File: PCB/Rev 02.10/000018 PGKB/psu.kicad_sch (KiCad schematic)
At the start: 11 parts, among them U6 MCP1825T-3302E/DC, U7 CAT811TTBI-GT3

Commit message: Maybe new psu needed
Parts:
- added U8: DC_DC_3V3_OKI-78SR-3.3/1.5-W36H-C, KD_Power_Supply:Converter_DCDC_Murata_OKI-78SR_Horizontal, symbol KD_Power_Supply:DC_DC_3V3_OKI-78SR-3.3/1.5-W36H-C
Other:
- note added: "Bigger PSU needed?"

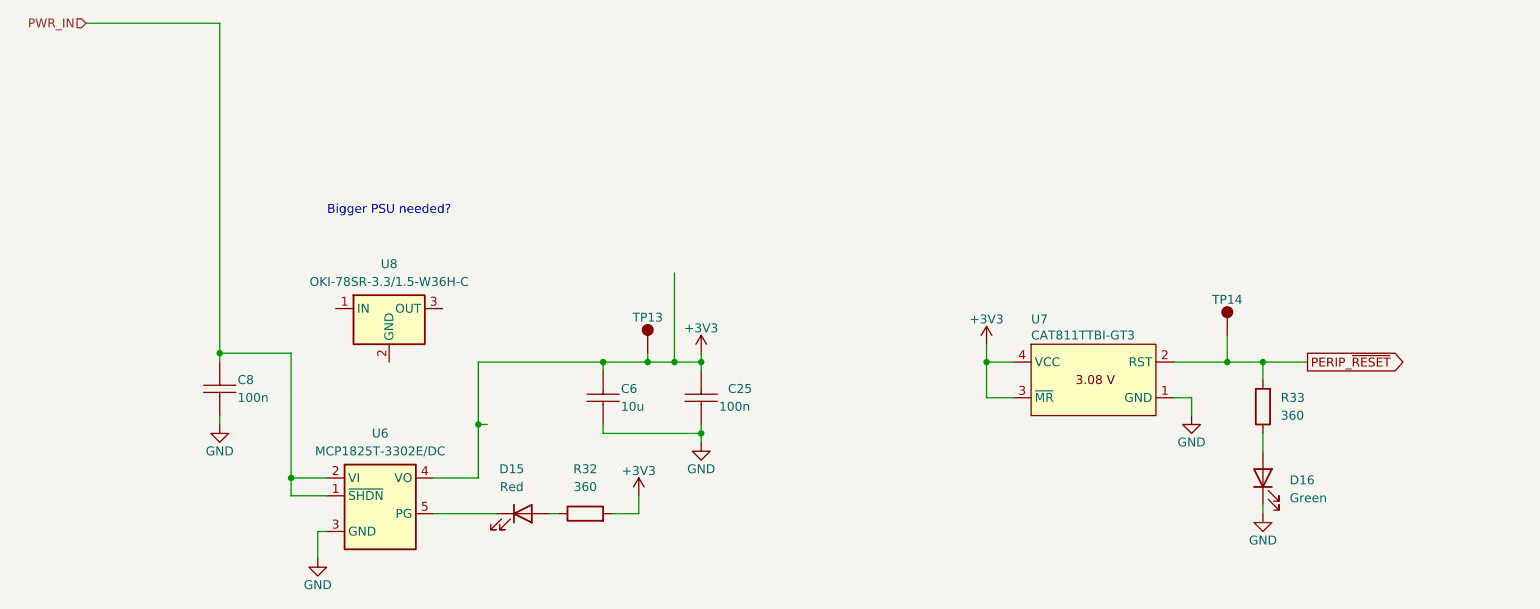
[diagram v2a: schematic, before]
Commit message: Bugfixes for Rev 2
Oscillator, USB reversed, USB series resistors values
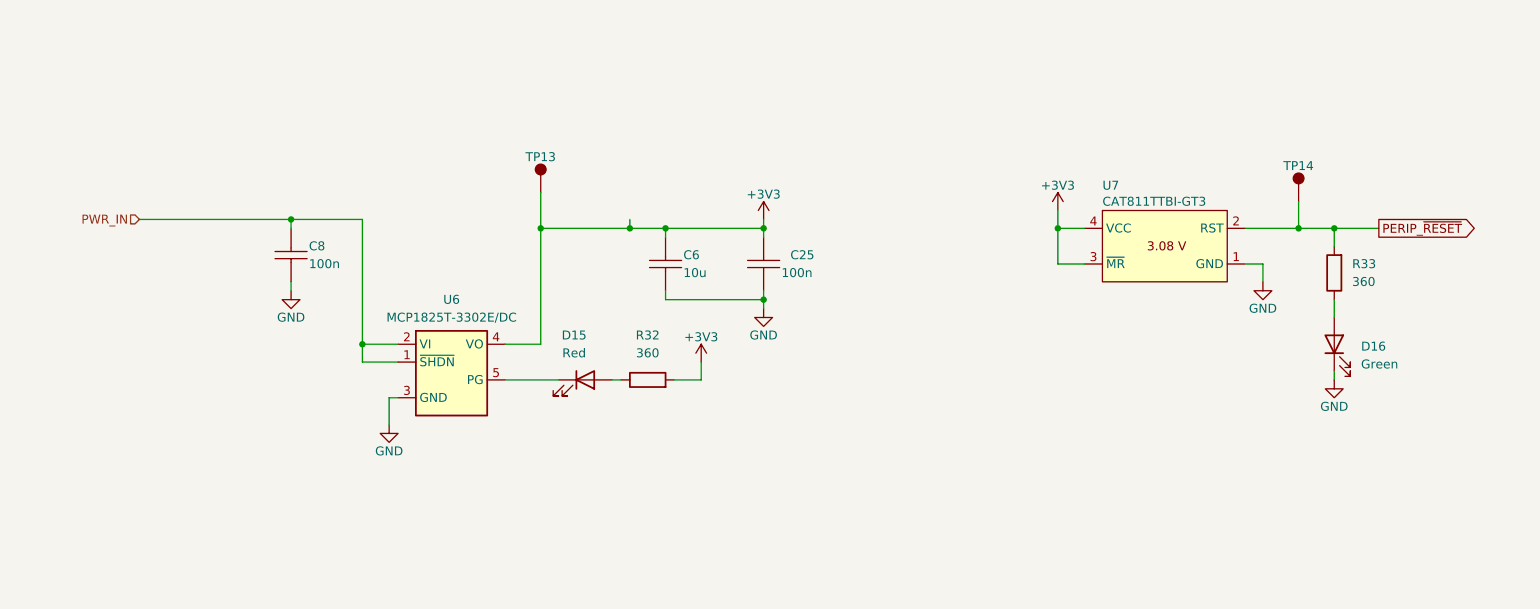
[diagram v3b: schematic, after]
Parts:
- removed U8: DC_DC_3V3_OKI-78SR-3.3/1.5-W36H-C, KD_Power_Supply:Converter_DCDC_Murata_OKI-78SR_Horizontal, symbol KD_Power_Supply:DC_DC_3V3_OKI-78SR-3.3/1.5-W36H-C
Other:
- note removed: "Bigger PSU needed?"
- moved on the sheet: C25, C6, C8, D15, D16, R32, R33, TP13, TP14, U6, U7

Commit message: Resolved DRC problems
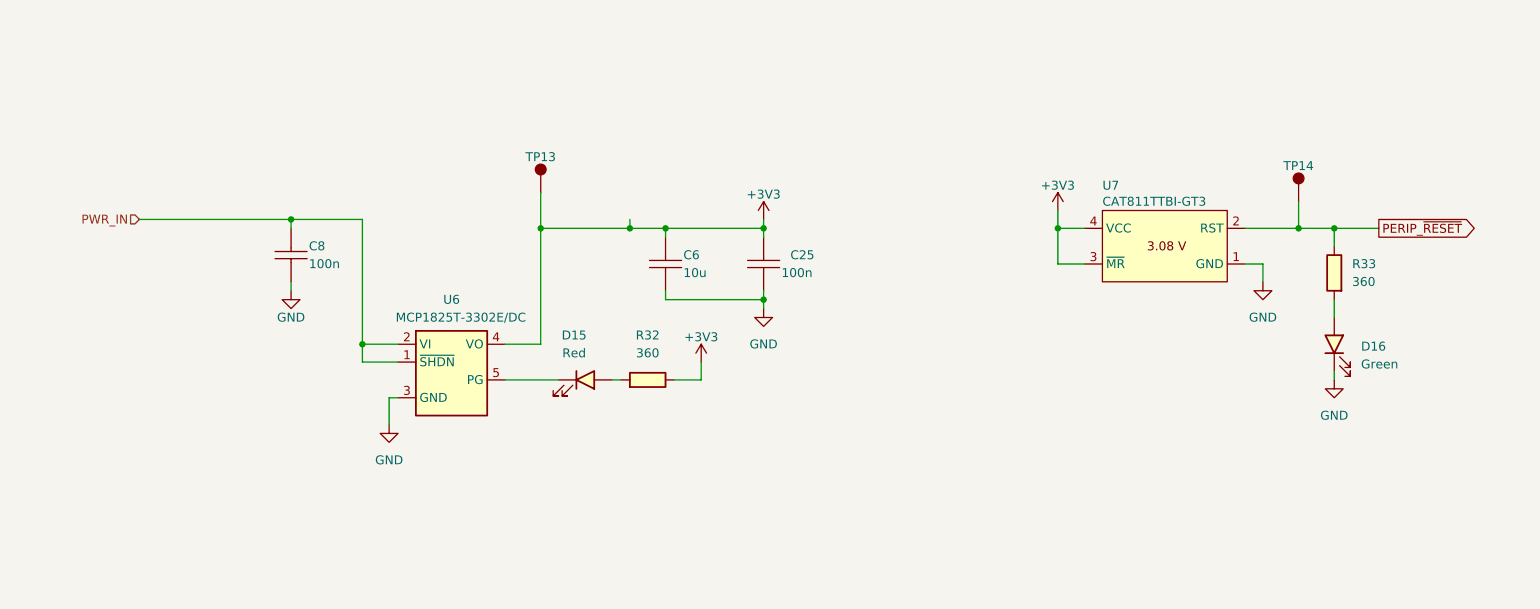
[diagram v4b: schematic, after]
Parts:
- R32, R33: value R_0603_360_1% -> 360; Code 360 -> (none)
- U6: symbol KD_IC_Regulator_DC_Converter:Regulator_3v3_500mA_0.5%_MCP1825T-3302E/DC -> KD_IC_Power_Supply:Regulator_3v3_500mA_0.5%_MCP1825T-3302E/DC
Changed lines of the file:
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@@
 		(fields_autoplaced yes)
 		(property "Reference" "R33"
-			(at 232.41 97.79 0)
+			(at 232.41 97.7899 0)
 			(effects
 				(font
@@
 			)
 		)
-		(property "Value" "R_0603_360_1%"
-			(at 242.57 130.81 0)
-			(effects
-				(font
-					(size 1.27 1.27)
-				)
-				(justify left)
-				(hide yes)
+		(property "Value" "360"
+			(at 232.41 100.3299 0)
+			(effects
+				(font
+					(size 1.27 1.27)
+				)
+				(justify right)
 			)
 		)
@@
 			)
 		)
-		(property "Description" ""
-			(at 229.87 99.06 0)
-			(effects
-				(font
-					(size 1.27 1.27)
-				)
-				(hide yes)
-			)
-		)
-		(property "Code" "360"
-			(at 232.41 100.33 0)
-			(effects
-				(font
-					(size 1.27 1.27)
-				)
-				(justify right)
+		(property "Description" "RES SMD 360 OHM 1% 1/10W 0603"
+			(at 242.57 133.858 0)
+			(effects
+				(font
+					(size 1.27 1.27)
+				)
+				(justify left top)
+				(hide yes)
 			)
 		)
@@
 		)
 		(property "Value" "GND"
-			(at 229.87 118.11 0)
+			(at 229.87 119.38 0)
 			(effects
 				(font
@@
 			)
 		)
-		(property "Description" ""
+		(property "Description" "Power symbol creates a global label with name \"GND\" , ground"
 			(at 229.87 114.3 0)
 			(effects
@@
 			)
 		)
-		(property "Value" "R_0603_360_1%"
-			(at 100.33 127 0)
-			(effects
-				(font
-					(size 1.27 1.27)
-				)
-				(justify left)
-				(hide yes)
+		(property "Value" "360"
+			(at 132.08 110.49 90)
+			(effects
+				(font
+					(size 1.27 1.27)
+				)
 			)
 		)
@@
 			)
 		)
-		(property "Description" ""
-			(at 132.08 114.3 0)
-			(effects
-				(font
-					(size 1.27 1.27)
-				)
-				(hide yes)
-			)
-		)
-		(property "Code" "360"
-			(at 132.08 110.49 90)
-			(effects
-				(font
-					(size 1.27 1.27)
-				)
+		(property "Description" "RES SMD 360 OHM 1% 1/10W 0603"
+			(at 97.282 127 0)
+			(effects
+				(font
+					(size 1.27 1.27)
+				)
+				(justify left top)
+				(hide yes)
 			)
 		)
@@
 			)
 		)
-		(property "Description" ""
+		(property "Description" "Power symbol creates a global label with name \"+3V3\""
 			(at 139.7 111.76 0)
 			(effects
@@
 		)
 		(property "Value" "GND"
-			(at 148.59 107.95 0)
+			(at 148.59 109.22 0)
 			(effects
 				(font
@@
 			)
 		)
-		(property "Description" ""
+		(property "Description" "Power symbol creates a global label with name \"GND\" , ground"
 			(at 148.59 104.14 0)
 			(effects
@@
 			)
 		)
-		(property "Description" ""
+		(property "Description" "CAP CER 0.1UF 50V X7R 0603"
 			(at 81.28 96.52 0)
 			(effects
@@
 			)
 		)
-		(property "Description" ""
+		(property "Description" "Power symbol creates a global label with name \"GND\" , ground"
 			(at 81.28 101.6 0)
 			(effects
@@
 	)
 	(symbol
-		(lib_id "KD_IC_Regulator_DC_Converter:Regulator_3v3_500mA_0.5%_MCP1825T-3302E/DC")
+		(lib_id "KD_IC_Power_Supply:Regulator_3v3_500mA_0.5%_MCP1825T-3302E/DC")
 		(at 104.14 109.22 0)
 		(unit 1)
@@
 		)
 		(property "Value" "MCP1825T-3302E/DC"
-			(at 104.14 105.41 0)
-			(do_not_autoplace yes)
+			(at 105.4656 105.41 0)
 			(effects
 				(font
@@
 			)
 		)
-		(property "Description" ""
-			(at 104.14 109.22 0)
-			(effects
-				(font
-					(size 1.27 1.27)
-				)
+		(property "Description" "Linear Voltage Regulator IC Positive Fixed 1 Output 500mA SOT-223-5"
+			(at 91.44 77.47 0)
+			(effects
+				(font
+					(size 1.27 1.27)
+				)
+				(justify left)
 				(hide yes)
 			)
@@
 		(fields_autoplaced yes)
 		(property "Reference" "D16"
-			(at 233.68 109.5375 90)
+			(at 233.68 109.5374 90)
 			(effects
 				(font
@@
 		)
 		(property "Value" "Green"
-			(at 233.68 112.0775 90)
+			(at 233.68 112.0774 90)
 			(effects
 				(font
@@
 			)
 		)
-		(property "Description" ""
+		(property "Description" "Green 525nm LED Indication - Discrete 3.3V 0603 (1608 Metric)"
 			(at 229.87 109.22 0)
 			(effects
@@
 			)
 		)
-		(property "Description" ""
+		(property "Description" "Capacitor"
 			(at 134.62 97.79 0)
 			(effects
@@
 			)
 		)
-		(property "Description" ""
+		(property "Description" "Test point"
 			(at 224.79 88.9 0)
 			(effects
@@
 			)
 		)
-		(property "Description" ""
+		(property "Description" "Red 624nm LED Indication - Discrete 2V 0603 (1608 Metric)"
 			(at 123.19 114.3 0)
 			(effects
@@
 			)
 		)
-		(property "Description" ""
+		(property "Description" "CAP CER 0.1UF 50V X7R 0603"
 			(at 148.59 97.79 0)
 			(effects
@@
 			)
 		)
-		(property "Description" ""
+		(property "Description" "Power symbol creates a global label with name \"+3V3\""
 			(at 148.59 91.44 0)
 			(effects
@@
 		)
 		(property "Value" "GND"
-			(at 95.25 124.46 0)
+			(at 95.25 125.73 0)
 			(effects
 				(font
@@
 			)
 		)
-		(property "Description" ""
+		(property "Description" "Power symbol creates a global label with name \"GND\" , ground"
 			(at 95.25 120.65 0)
 			(effects
@@
 			)
 		)
-		(property "Description" ""
+		(property "Description" "Test point"
 			(at 116.84 87.63 0)
 			(effects
@@
 		)
 		(property "Value" "GND"
-			(at 219.71 104.14 0)
+			(at 219.71 105.41 0)
 			(effects
 				(font
@@
 			)
 		)
-		(property "Description" ""
+		(property "Description" "Power symbol creates a global label with name \"GND\" , ground"
 			(at 219.71 100.33 0)
 			(effects
@@
 			)
 		)
-		(property "Description" ""
+		(property "Description" "Power symbol creates a global label with name \"+3V3\""
 			(at 190.5 90.17 0)
 			(effects
@@
 			)
 		)
-		(property "Description" ""
+		(property "Description" "IC SUPERVISOR 1 CHANNEL SOT143 3.08V"
 			(at 194.31 92.71 0)
 			(effects
